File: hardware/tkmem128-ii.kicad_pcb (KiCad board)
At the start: 4 copper layers, 78.7 x 66 mm, 21 parts, among them J1 Barramento TK, U1 GAL20V8B, U2 74HCT273, U3 AS6C1008-55PCN, U4 27C256

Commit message: Projeto passa a se chamar TKMEM-128 II
"TKMEM-128 KiCad" dizia so que mudou de software de CAD, quando na verdade a
placa e outra: 4 camadas, trilha do dobro, roteamento e posicionamento refeitos,
JP4 e SJ1/SJ2 fora, auto-desativacao em outro pino, compatibilidade com o ZX
Spectrum recuperada. "II" nomeia a geracao, e manter "TKMEM-128" no nome mantem
a linhagem visivel.

O CUIDADO PRINCIPAL foi nao apagar o credito. "TKMEM-128" aparece no repositorio
nos dois sentidos, e so o primeiro virou "II":

  a NOSSA placa  titulo do README, serigrafia das duas placas, gal/README, duas
                 frases do PREPARAR-O-TK
  a do LUCCAS    a linha da tabela de derivacao, o diagrama de linhagem, "o autor
                 da TKMEM-128 original deixou de fornecer a ROM", e o titulo do
                 artigo dele citado no PREPARAR-O-TK — esses ficaram intactos

Uma substituicao global teria reescrito a atribuicao, que e justamente o que a
CERN-OHL-S existe para proteger.

ARQUIVOS. Os do projeto KiCad seguiram o nome:

  hardware/tkmem128.kicad_{pro,sch,pcb,dru}          -> tkmem128-ii.*
  hardware/expansor/tkmem128-expansor.*             -> tkmem128-ii-expansor.*
  gerbers                                            -> tkmem128-ii-F_Cu.gbr etc.

A BIBLIOTECA NAO. `hardware/lib/tkmem128.pretty` e `tkmem128.kicad_sym` continuam
com o nome antigo de proposito: sao um acervo de footprints do barramento do TK,
nao do projeto, e renomea-las obrigaria a reescrever o prefixo `tkmem128:` em
cada componente das duas placas — superficie de erro sem ganho. Mesmo raciocinio
para `hardware/gal/tkmem128.pld/.jed`, que e o mapa de fusiveis herdado.

Repositorio renomeado para github.com/lrrosa/tkmem128-ii (o GitHub redireciona o
endereco antigo). A URL na serigrafia das duas placas acompanhou.

De quebra: com tres caracteres a mais, o titulo na serigrafia da principal — que
e centralizado — cresceu para os dois lados e encostou em R4. Deslocado 5 mm.

DRC 0/0 na principal, 0 violacoes na t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
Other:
- board text added: "TKMEM-128 II LRRosa 2026 v1.0"
- board text added: "github.com/lrrosa/tkmem128-ii"
- board text removed: "TKMEM-128 LRRosa 2026 v1.0"
- board text removed: "github.com/lrrosa/tkmem128-kicad"
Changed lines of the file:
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@@
 		)
 	)
-	(gr_text "TKMEM-128   LRRosa 2026 v1.0"
-		(at 22 53 0)
+	(gr_text "TKMEM-128 II   LRRosa 2026 v1.0"
+		(at 27 53 0)
 		(layer "F.SilkS")
 		(effects
@@
 		)
 	)
-	(gr_text "github.com/lrrosa/tkmem128-kicad"
+	(gr_text "github.com/lrrosa/tkmem128-ii"
 		(at 20.5 12 0)
 		(layer "B.SilkS")

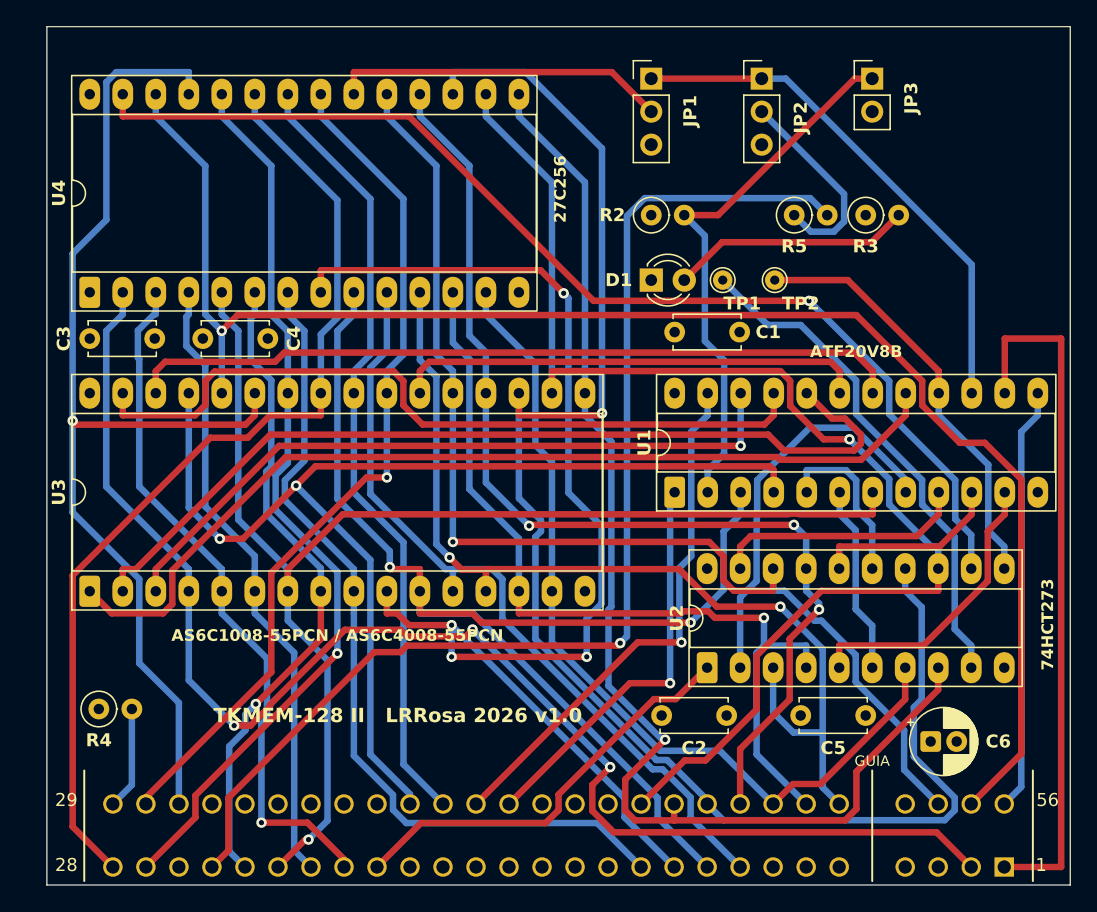
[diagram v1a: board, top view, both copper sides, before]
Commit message: Sobe J1 1,5 mm e abre o furo de fixacao H1
A fileira de baixo do conector estava a 1,385 mm da aresta — 0,635 mm de cobre
ate a borda — e o corpo do conector, que tem 10 mm de fundo, sobrava 1,19 mm
PARA FORA da placa: o contorno cortava o conector ao meio, e por isso a
serigrafia dele era um "U" aberto. Subindo 1,5 mm (medida conferida contra
interfaces reais de TK90X) o cobre fica a 2,135 mm da aresta, o corpo termina
0,31 mm DENTRO da placa e o retangulo da serigrafia fecha.

Isso obrigou a rerotear: das 33 pontas de trilha que pousavam em ilhas de J1,
26 saiam a 45 graus costurando ENTRE as ilhas, entao subir a fileira jogava as
ilhas para dentro do proprio leque. Aproveitei o rerroteamento para abrir H1,
o furo de fixacao da torre superior da caixa Patola, em (39,37 ; 4,02) —
posicao conferida contra a peca real em impressao 1:1. Na placa de 2 camadas
ele custava duas ligacoes; agora coube.

Resultado: 74/74 nets, DRC 0/0, ERC 0. F.Cu 1408,5 mm e B.Cu 1596,7 mm em 33
vias (eram 39).

Detalhes que valem registro:

- H1 e Ø2,7 porque acima disso o furo entra no courtyard do soquete de U4, a
  1,42 mm. O cobre nao e o limite (sobra 0,72 mm ate U4.15); o soquete e.
- H1 nao tem courtyard de proposito: a folga da cabeca do parafuso NAO cabe, e
  declarar uma seria mentir. Documentado em ANTES-DE-FABRICAR e MONTAGEM.
- A area de exclusao de raio 1,85 nas 4 camadas afasta os planos de GND e +5V
  0,5 mm da parede do furo. Sem ela o recuo seria so os 0,25 da regra, e
  parafuso metalico raspando a parede pode arrastar cobre de um plano ao outro.
  Ela tambem e o que o Freerouting enxerga como keepout no DSN.
- O footprint do furo vem da biblioteca do projeto, nao montado a mao: sem FPID
  o exportador Specctra escreve (component "") e o KiCad se recusa a reimportar
  o .ses; montado a mao, o DRC acusa lib_footprint_mismatch para sempre.
- A biblioteca estava com ilha de 1,75 mm no conector — o valor que era o
  gargalo do roteamento — enquanto a placa ja usava 1,50. Qu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
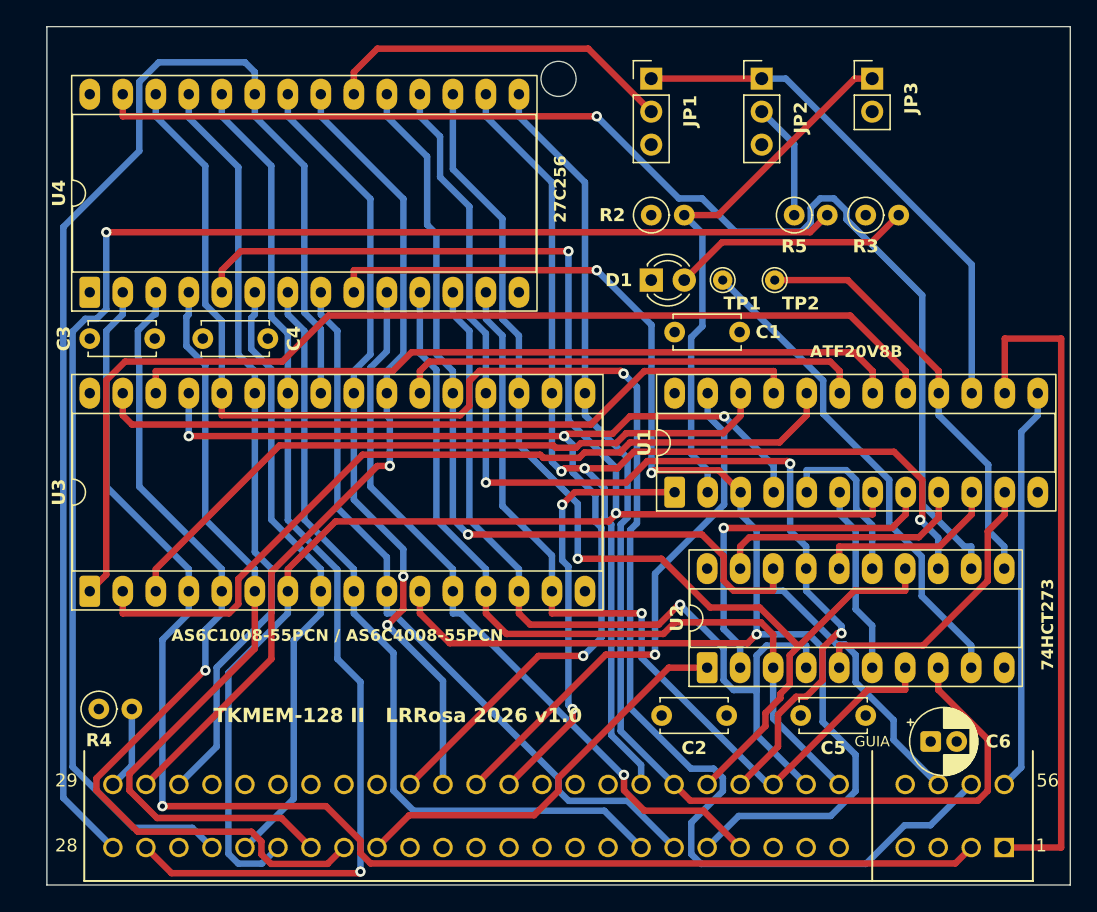
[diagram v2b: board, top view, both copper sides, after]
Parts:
- added H1: MountingHole_2.7mm, tkmem128:MountingHole_2.7mm, F.Cu at (39.4, 4.02)
- moved J1 1.50 mm to (39.4, 60.7)
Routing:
- net A2: track 96.4 -> 56.9 mm, vias 4 -> 0
- net D5: track 123.1 -> 84.7 mm
- net A5: track 99.4 -> 127.5 mm, vias 1 -> 2
- net A8: track 84.5 -> 58.7 mm, vias 1 -> 0
- net A11: track 75.8 -> 99.5 mm
- net A1: track 94.6 -> 116.5 mm, vias 2 -> 3
- net ROMCS_BUS: track 90.5 -> 112.0 mm
- net A7: track 53.7 -> 67.8 mm
- net A6: track 48.3 -> 60.4 mm
- net A9: track 70.0 -> 81.6 mm
- net D0: track 75.0 -> 64.0 mm, vias 2 -> 0
- net SA18: track 73.2 -> 83.8 mm
- net ROMA14: track 86.2 -> 95.0 mm
- net A13: track 120.0 -> 127.3 mm
- net ROMCS_DRV: track 15.8 -> 9.00 mm
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
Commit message: H1 vira passagem da TORRE (Ø5,4), e a serigrafia dos jumpers vira tabela
O FURO. H1 nasceu Ø2,7, dimensionado como furo de parafuso. Errado: no desenho
PB 085/3_TP a torre da caixa tem Ø5 EXTERNO — o Ø2,5 e o furo-piloto dentro
dela — e a placa assenta no fundo da tampa, que e de onde a torre nasce. Com
Ø2,7 a placa nao desce, para em cima da torre. O furo tem que deixar passar a
TORRE, nao o parafuso. Ø5,4 da 0,2 mm de folga radial, que a conicidade de
desmoldagem pede: e a base da torre, a parte mais larga, que encontra a placa.

Some junto com o furo pequeno todo o problema que ele criava: o parafuso agora
corre dentro da torre e nunca toca a placa, entao nao ha questao de folga para
a cabeca nem risco de parafuso metalico raspar a parede e encostar o plano de
GND no de +5V. H1 virou pino de localizacao; quem segura continua sendo o EVA.

Custou U4 recuar 1,5 mm para a esquerda e outro rerroteamento. Depois do
recuo: 0,60 mm entre o cobre de U4 e a aresta (regra 0,30) e 2,91 mm entre o
soquete e o furo. 74/74 nets, DRC 0/0, ERC 0, agora com 21 vias (eram 33) e
F.Cu 1546,4 / B.Cu 1524,5 mm.

O canal acima do furo praticamente fechou — 0,22 mm de janela para o centro de
uma trilha, contra 1,37 mm com Ø2,7 — e o roteador deu a volta sozinho. Mas o
otimo de isolacao no DSN mudou de 0,213 para 0,215: varrer de novo a cada
mudanca de placa, nao reaproveitar o valor.

A SERIGRAFIA. As tres legendas de uma linha viraram tabelas no verso, no
formato que o Leonardo desenhou. Com a placa na mao e um shunt na pinca, linha
corrida nao serve — nao da para achar a posicao de relance.

Detalhe que so aparece no render: no verso a leitura e espelhada, entao a
ordem em coordenada de placa tem que ser a inversa da que se quer ver. Na
primeira tentativa saiu JP3, JP2, JP1 com a coluna da posicao a direita.

O titulo virou duas linhas: TKMEM-128 II a 2,2 mm (era 1,10) e o credito a
1,1 embaixo. Em uma linha so nao passava de 1,35 — a faixa livre da face de
cima tem 37 mm e os 31 cara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
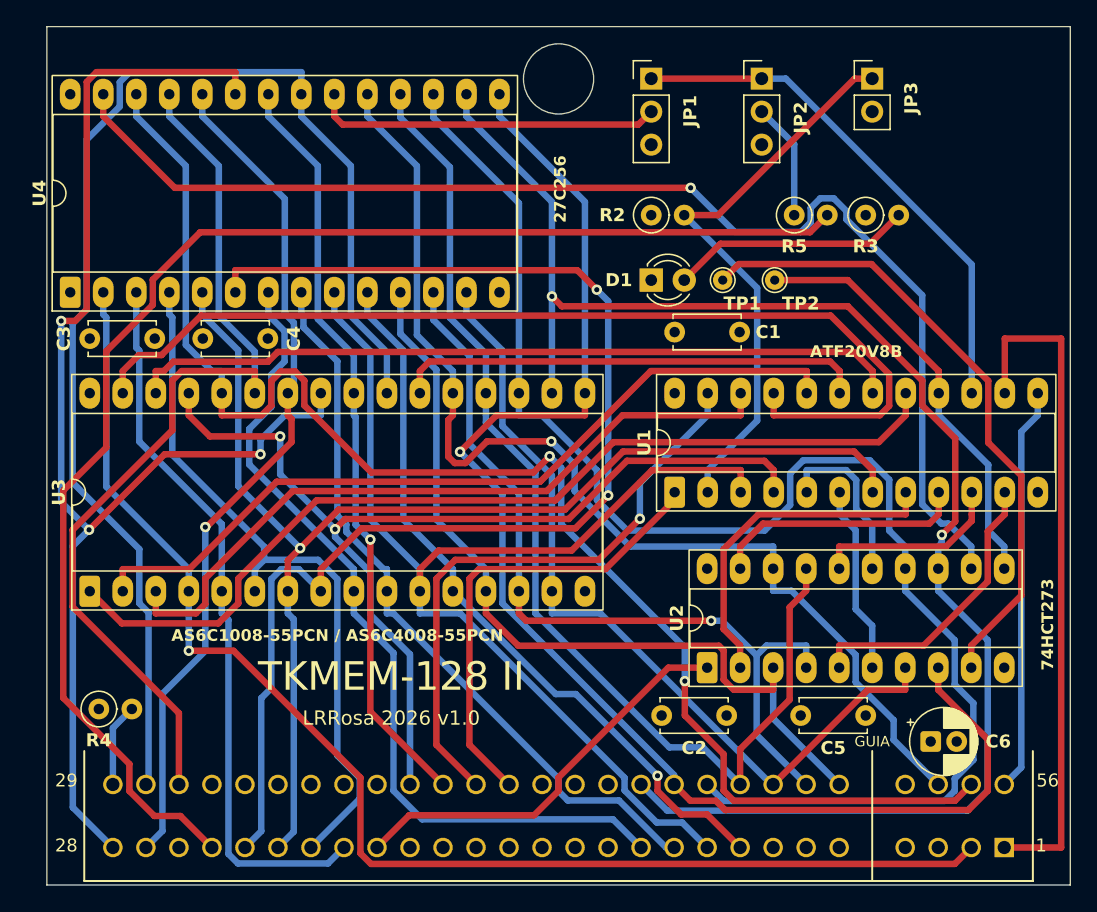
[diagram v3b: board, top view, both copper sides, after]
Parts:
- H1: value MountingHole_2.7mm -> MountingHole_5.4mm; footprint tkmem128:MountingHole_2.7mm -> tkmem128:MountingHole_5.4mm
- moved U4 1.50 mm to (1.80, 20.4)
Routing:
- net A4: track 47.5 -> 98.8 mm, vias 0 -> 2
- net A10: track 64.7 -> 99.8 mm, vias 1 -> 0
- net A5: track 127.5 -> 96.3 mm, vias 2 -> 1
- net A1: track 116.5 -> 88.8 mm, vias 3 -> 0
- net D5: track 84.7 -> 112.3 mm, vias 1 -> 0
- net D4: track 94.3 -> 119.7 mm, vias 3 -> 2
- net SA15: track 55.5 -> 77.6 mm
- net A9: track 81.6 -> 65.8 mm
- net A13: track 127.3 -> 111.6 mm, vias 1 -> 2
- net A8: track 58.7 -> 71.7 mm
- net D3: track 94.5 -> 107.2 mm, vias 0 -> 1
- net A7: track 67.8 -> 55.8 mm, vias 1 -> 0
- net VRAM: track 37.7 -> 49.4 mm
- net SA18: track 83.8 -> 73.2 mm
- net WR_N: track 88.7 -> 78.2 mm, vias 4 -> 2
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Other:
- board text added: "1-2"
- board text added: "128K"
- board text added: "2-3"
- board text added: "512K"
- board text added: "ABERTO"
- board text added: "FECHADO"
- board text added: "JP1"
- board text added: "JP2"
- board text added: "JP3"
- board text added: "LRRosa 2026 v1.0"
- board text added: "ROM INTERNA"
- board text added: "ROM TKMEM"
- board text added: "ROMCS HIGH"
- board text added: "ROMCS LOW"
- board text added: "TKMEM-128 II"
- board text removed: "JP1 1-2 = ROM 128 | 2-3 = ROM do TK"
- board text removed: "JP2 aberto = ROM do TK | 1-2 = pelo GAL | 2-3 = +5V"
- board text removed: "JP3 fechado = 512K (AS6C4008)"
- board text removed: "TKMEM-128 II LRRosa 2026 v1.0"

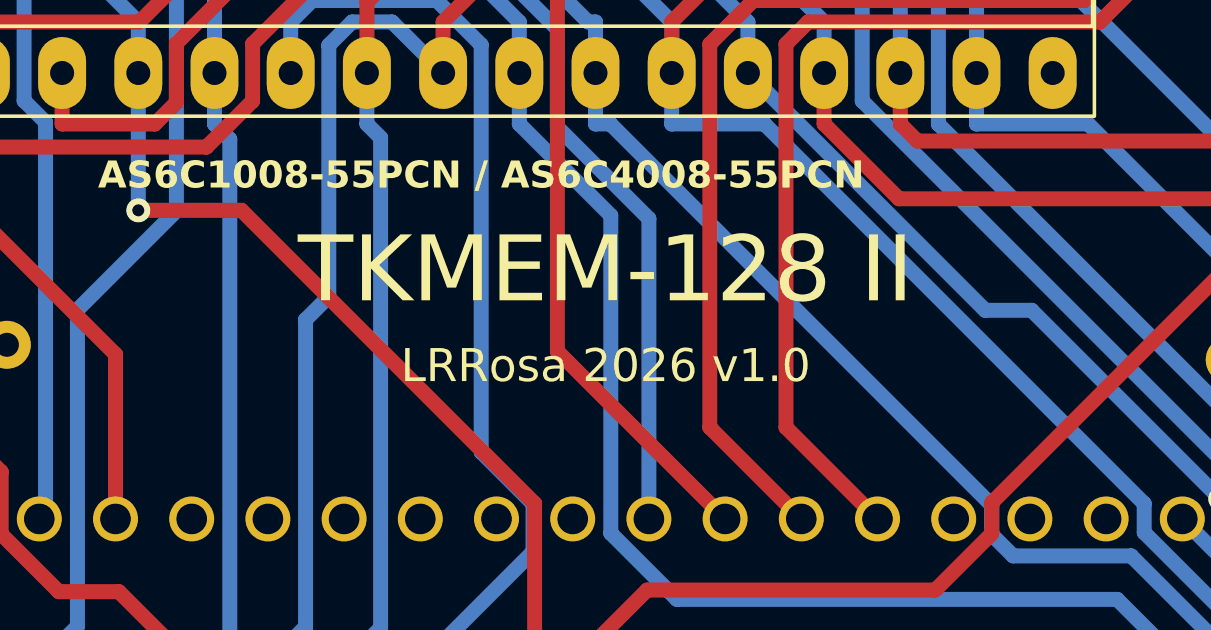
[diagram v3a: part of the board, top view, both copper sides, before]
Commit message: Realoja as tabelas dos jumpers e afasta o titulo do silk de cima
JP2 e JP3 foram para o meio do canal de U3 (y 29,00..42,64, 13,64 mm entre as
duas fileiras de pinos do soquete), centrados nele. JP1 subiu para a faixa
livre acima de U1, entre os pontos de teste e a fileira de cima do soquete
(x 54..77, y 17..27). Sao os unicos retangulos grandes da placa: no verso nada
cobre o canal de um DIP, e o resto esta tomado por ilhas passantes, que
existem nas duas faces.

Em JP2, "1-2 = ROMCS LOW" virou "1-2 = ROMCS GAL". Aquela posicao nao fixa
nivel nenhum: ela liga o ROMCS do barramento a saida do GAL. Quem fixa nivel e
a 2-3, em +5V, e essa continua "ROMCS HIGH".

O titulo desceu 0,7 mm — colava no silk de U3 — e o credito subiu de 1,1 para
1,4 mm. Agora sobram 2,0 mm ate a linha "AS6C1008-55PCN / AS6C4008-55PCN" e
0,9 mm ate o contorno de J1.

Duas correcoes no proprio script, que so apareceram ao repetir:

- a faixa de limpeza estava presa em y 28,5..37, onde as tabelas estavam
  ANTES; movendo-as, a rodada seguinte teria desenhado por cima em vez de
  substituir. Agora cobre y 18..42,5, conferido item a item: nessa faixa o
  verso nao tem mais nada.
- o titulo era casado so por "TKMEM-128 II", entao a linha do credito ficava
  para tras e a rodada seguinte empilhava outra por cima — deu um
  silk_overlap de 'LRRosa 2026 v1.0' com ele mesmo.

DRC 0/0, os quatro conferidores OK.

Co-Authored-By: Claude Opus 5 <noreply@anthropic.com>
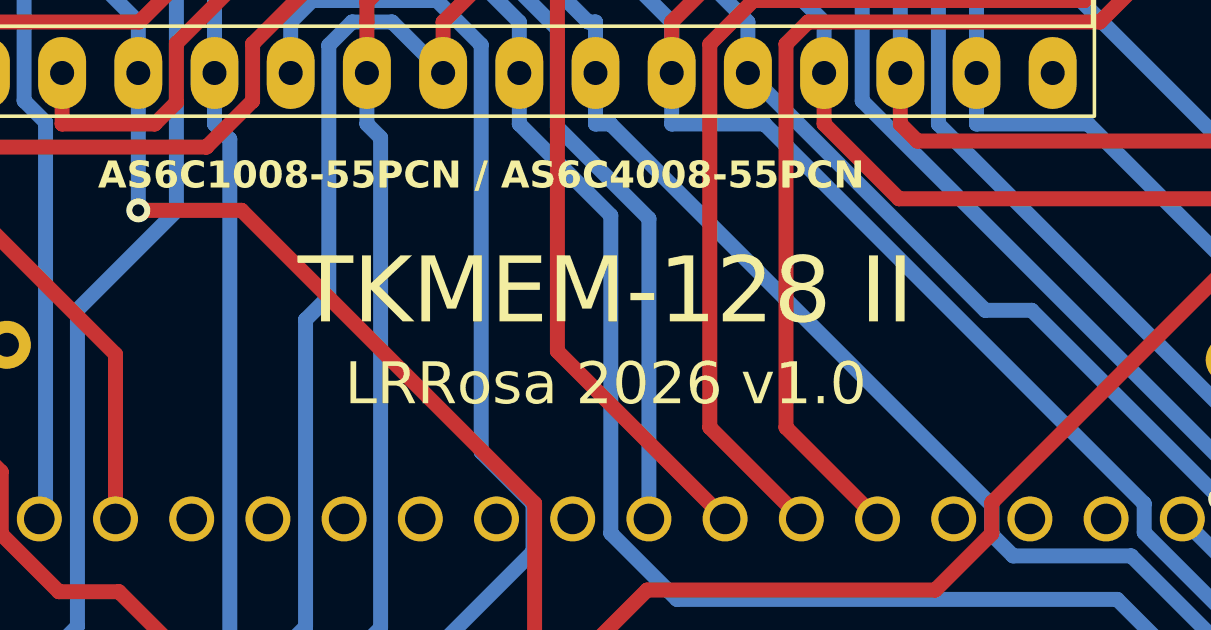
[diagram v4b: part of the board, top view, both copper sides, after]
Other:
- board text added: "ROMCS GAL"
- board text removed: "ROMCS LOW"
